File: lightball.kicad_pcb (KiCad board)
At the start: 2 copper layers, 42.6 x 20.3 mm, 48 parts, among them J1 IN, J2 Conn_01x06, J3 Motor, Q1 2N7002, U1 BMP388, U2 MIC5504-3.3YM5, U3 ACT4088, U4 ESP8266EX, U5 25LCxxx, Y1 Crystal

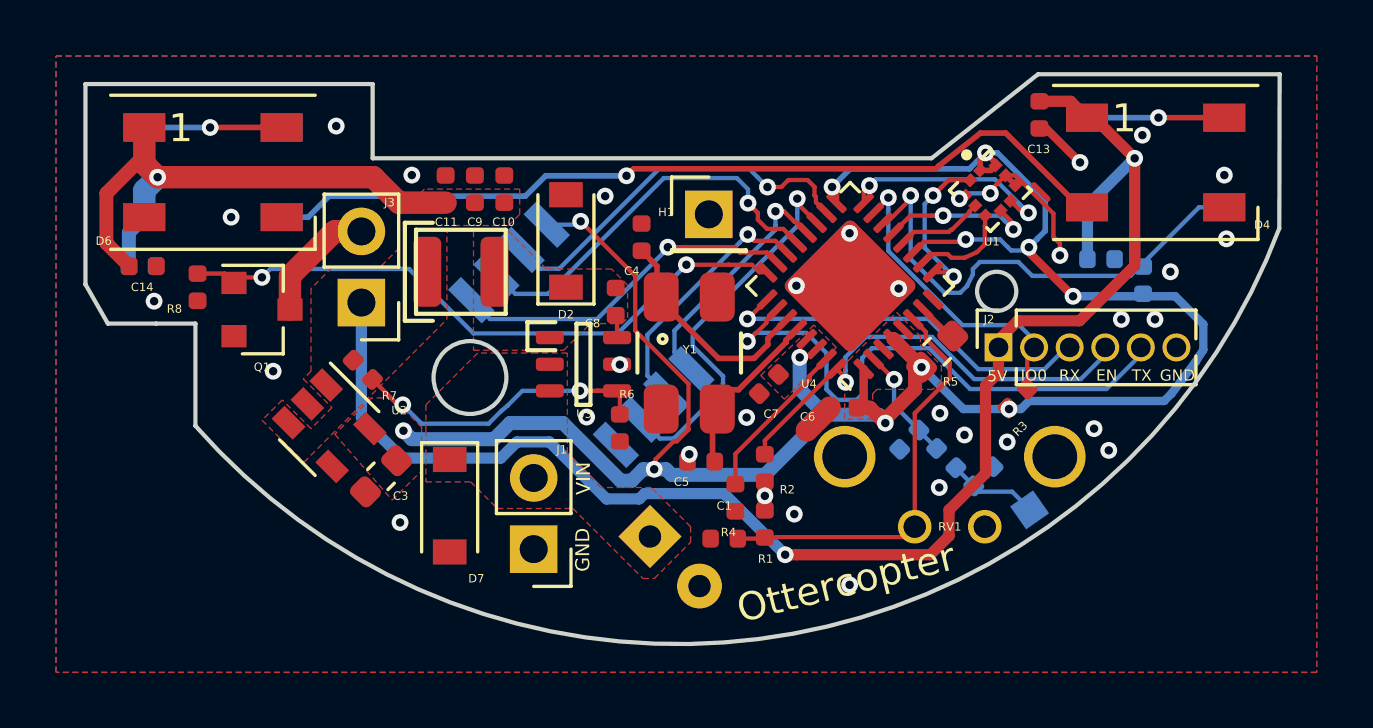
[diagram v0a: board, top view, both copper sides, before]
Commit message: FIX: better ground connection
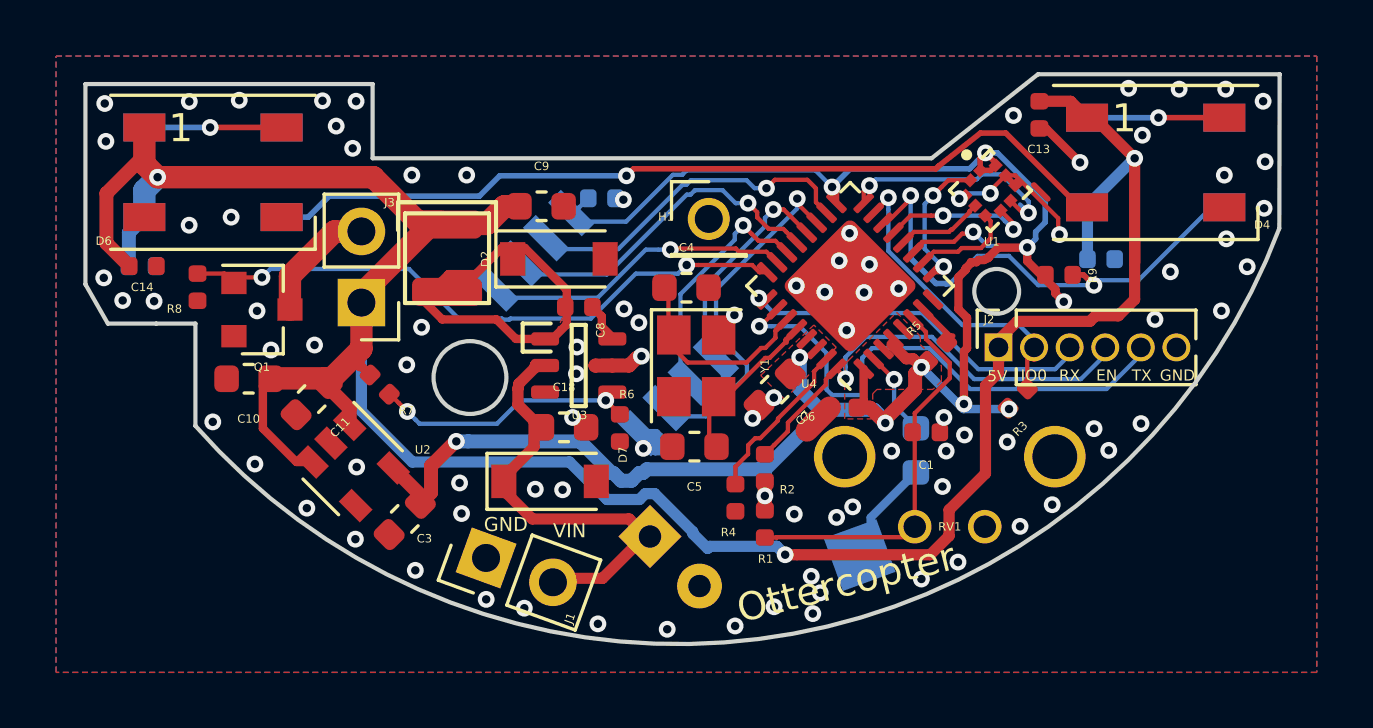
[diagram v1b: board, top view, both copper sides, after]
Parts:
- removed C16, C17: C_Small, Capacitor_SMD:C_0402_1005Metric
- removed G***: LOGO, otter:ottercopter
- added C18: 1u, Capacitor_SMD:C_0603_1608Metric, F.Cu at (87.1, 117.3)
- added C19: 0.1µ, Capacitor_SMD:C_0402_1005Metric, B.Cu at (88.5, 109.1)
- C10, C11, C4, C5: footprint Capacitor_SMD:C_0402_1005Metric -> Capacitor_SMD:C_0603_1608Metric
- C15: value 0.1µ -> 10u
- C7, C9: value 0.1µ -> 10u; footprint Capacitor_SMD:C_0402_1005Metric -> Capacitor_SMD:C_0603_1608Metric
- L2: footprint Inductor_SMD:L_0402_1005Metric -> Inductor_SMD:L_0603_1608Metric
- R5: footprint Resistor_SMD:R_0603_1608Metric -> Resistor_SMD:R_0402_1005Metric
- R9: moved to F.Cu
- Y1: value Crystal -> Crystal_GND24; footprint stmbl:Crystal_SMD_0603_4Pads -> Crystal:Crystal_SMD_SeikoEpson_FA238-4Pin_3.2x2.5mm
- moved C10 11.4 mm to (75.9, 115.5), turned to 180 degrees
- moved C11 8.89 mm to (78.1, 116.2), turned to 225 degrees
- moved C1 8.15 mm to (100.1, 117.4), turned to 180 degrees
- moved AE1 6.28 mm to (97.7, 121.8), turned to 20 degrees
- moved D7 3.69 mm to (86.6, 119.2), turned to 0 degrees
- moved R9 3.01 mm to (104.8, 111.8), turned to 180 degrees
- moved C9 2.46 mm to (86.3, 109.4), turned to 0 degrees
- moved C4 2.41 mm to (91.5, 112.3), turned to 0 degrees
- moved C3 1.74 mm to (81.4, 120.5)
- moved J1 1.73 mm to (84.3, 121.9), turned to 70 degrees
- moved U2 1.63 mm to (79.6, 118.6)
- moved C8 1.33 mm to (87.7, 113.0), turned to 0 degrees
- moved L2 1.12 mm to (99.7, 118.1), turned to 90 degrees
- moved U5 0.97 mm to (88.6, 113.5)
- moved R7 0.80 mm to (80.6, 115.7)
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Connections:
- U4 pad 5: +3V3 -> Net-(U4-Pad5)
- Y1 pad 2: Net-(C5-Pad1) -> GNDD
- Y1 pad 3: (no net) -> Net-(C5-Pad1)
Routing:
- net +5V: track 76.7 -> 96.4 mm
- net VPP: track 0.00 -> 15.1 mm
- net Net-(C8-Pad1): track 0.00 -> 13.6 mm
- net +3V3: track 80.8 -> 75.7 mm, vias 13 -> 12
- net GNDD: track 10.5 -> 14.6 mm, vias 32 -> 92
- net Net-(U4-Pad21): track 14.1 -> 11.6 mm
- net Net-(U4-Pad18): track 13.8 -> 11.8 mm
- net Net-(U4-Pad23): track 12.5 -> 10.5 mm
- net Net-(U4-Pad19): track 13.9 -> 12.2 mm
- net Net-(R6-Pad1): track 10.9 -> 9.51 mm
- net Net-(U4-Pad20): track 8.82 -> 7.43 mm
- net TXD: track 20.5 -> 19.2 mm
- net Net-(U4-Pad22): track 9.14 -> 8.10 mm
- net ADC: track 15.0 -> 14.1 mm
- net Net-(L2-Pad2): track 4.13 -> 3.24 mm
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- removed copper zone on F.Cu, net +5V
- removed copper zone on F.Cu, net VPP
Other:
- outline, holes or cut-outs redrawn

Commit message: Fix DRC violation
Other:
- net class Default: clearance 0.2 -> 0.154; trace_width 0.2 -> 0.154
- rule trace_clearance: 0.2 -> 0.154

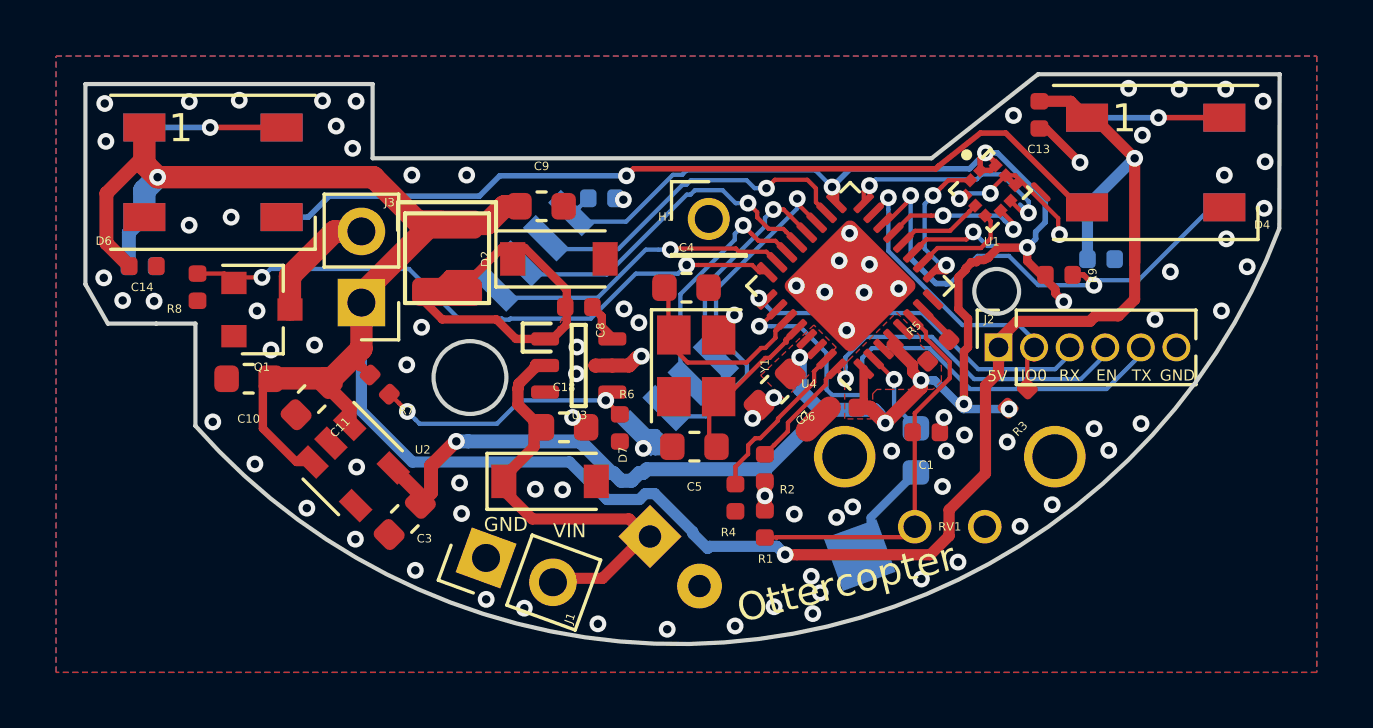
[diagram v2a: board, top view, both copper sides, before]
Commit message: closed dome island in the copper planes
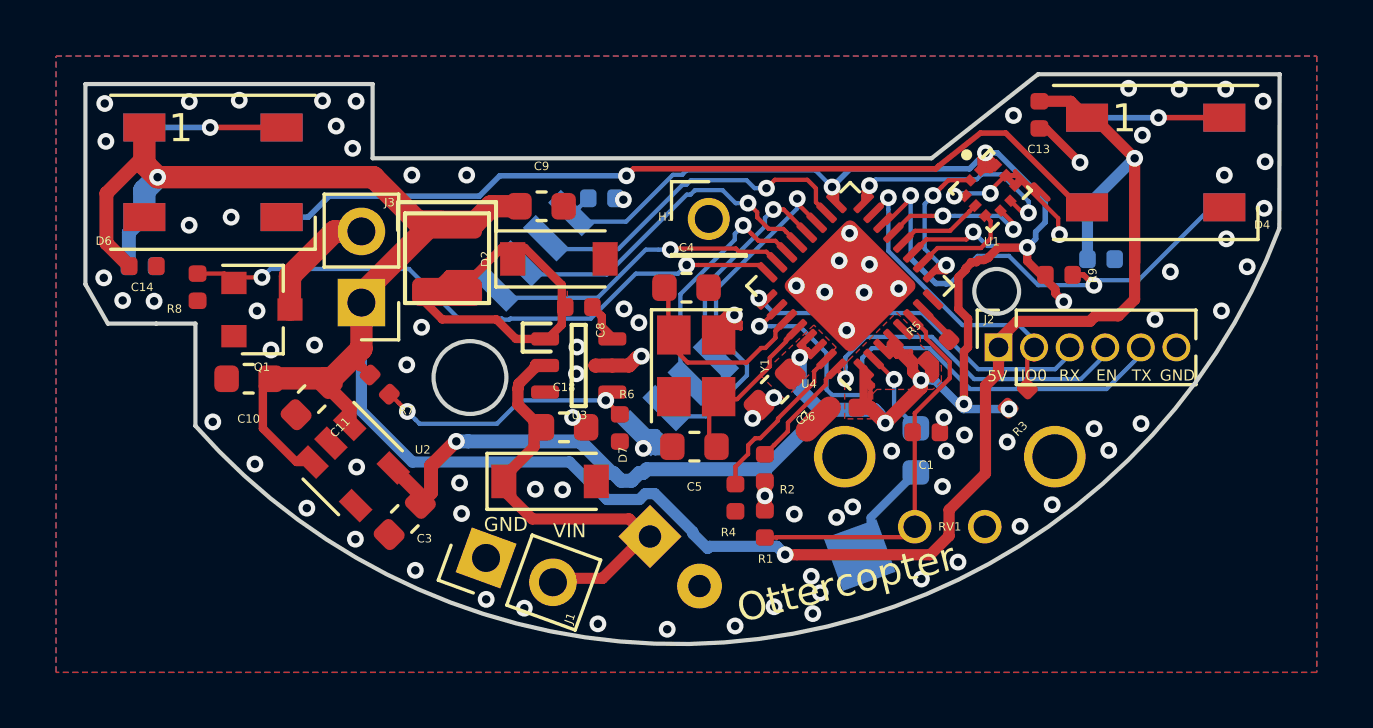
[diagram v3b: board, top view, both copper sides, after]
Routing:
- net +3V3: track 75.4 -> 83.4 mm
- net GNDD: track 14.6 -> 19.1 mm
